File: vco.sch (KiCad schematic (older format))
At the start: 0 parts

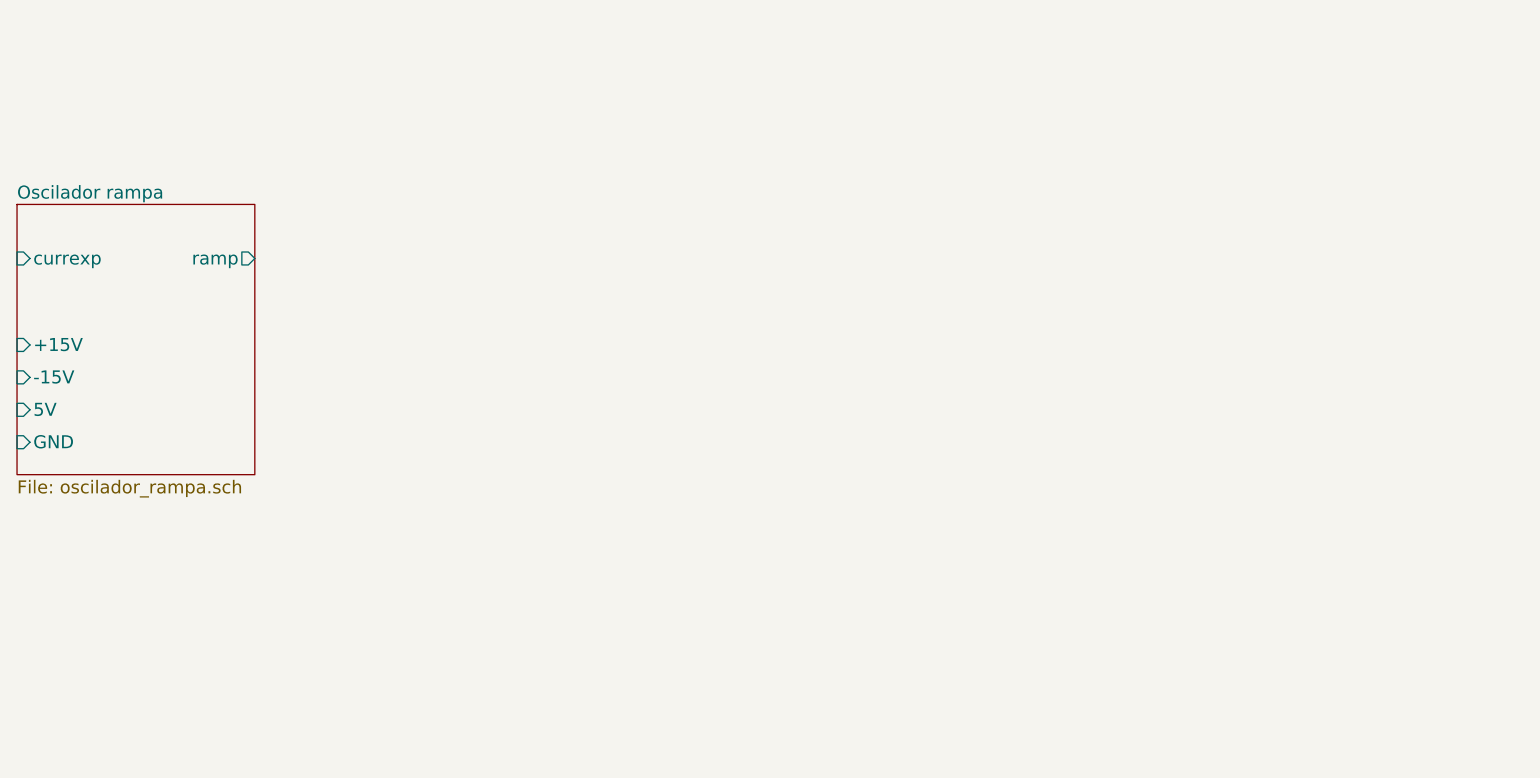
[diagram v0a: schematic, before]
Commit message: añado el conversor exponencial y mezclador
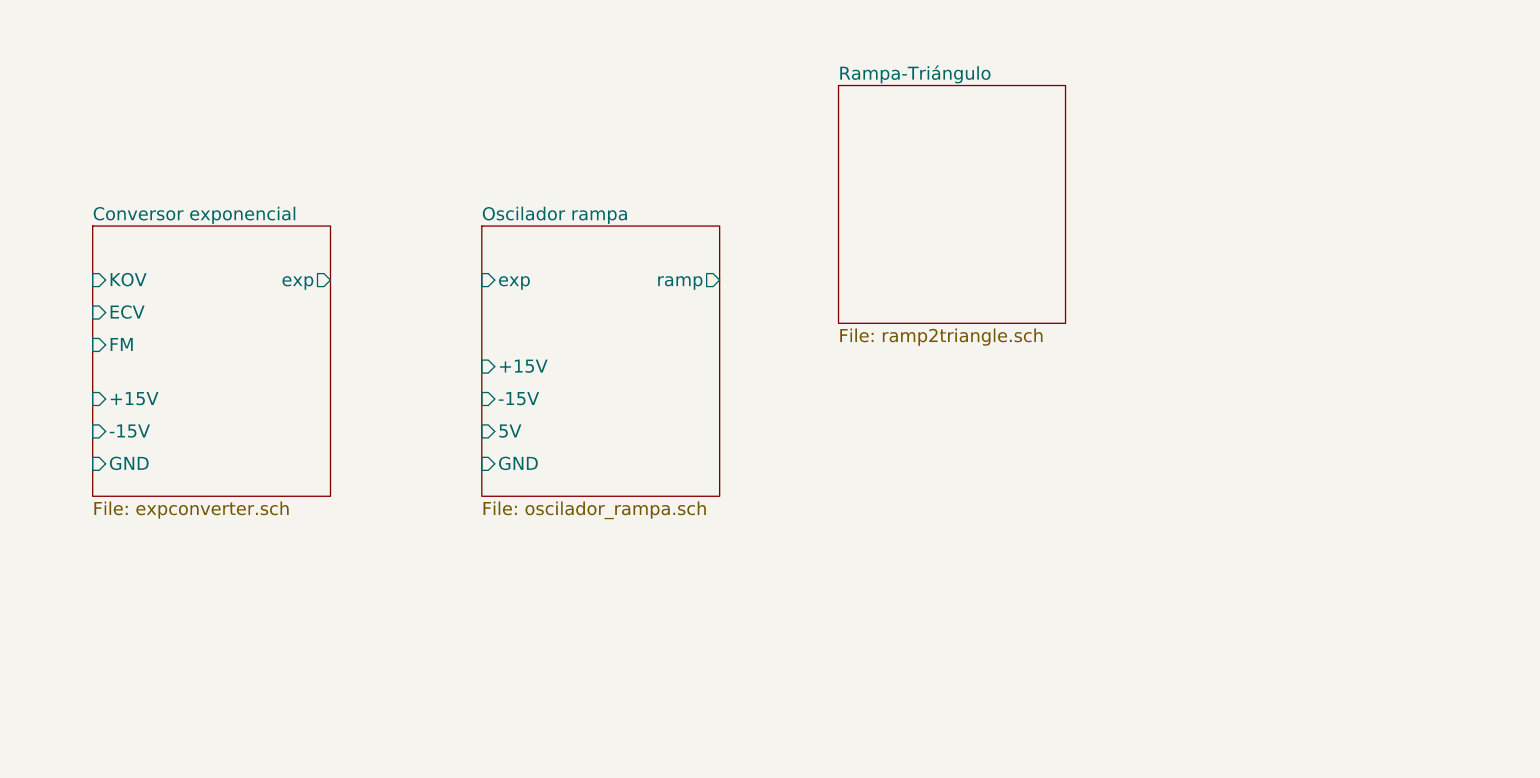
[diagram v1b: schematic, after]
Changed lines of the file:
@@
 $Descr A4 11693 8268
 encoding utf-8
-Sheet 1 2
+Sheet 1 4
 Title "Voltage Controlled Oscillator"
 Date ""
@@
 $EndDescr
 $Sheet
-S 3500 2500 1100 1250
+S 5650 2600 1100 1250
 U 59D4DFBE
 F0 "Oscilador rampa" 60
 F1 "oscilador_rampa.sch" 60
-F2 "currexp" I L 3500 2750 60
-F3 "GND" I L 3500 3600 60
-F4 "5V" I L 3500 3450 60
-F5 "ramp" O R 4600 2750 60
-F6 "+15V" I L 3500 3150 60
-F7 "-15V" I L 3500 3300 60
+F2 "exp" I L 5650 2850 60
+F3 "GND" I L 5650 3700 60
+F4 "5V" I L 5650 3550 60
+F5 "ramp" O R 6750 2850 60
+F6 "+15V" I L 5650 3250 60
+F7 "-15V" I L 5650 3400 60
+$EndSheet
+$Sheet
+S 3850 2600 1100 1250
+U 59D54B94
+F0 "Conversor exponencial" 60
+F1 "expconverter.sch" 60
+F2 "GND" I L 3850 3700 60
+F3 "KOV" I L 3850 2850 60
+F4 "ECV" I L 3850 3000 60
+F5 "FM" I L 3850 3150 60
+F6 "exp" O R 4950 2850 60
+F7 "+15V" I L 3850 3400 60
+F8 "-15V" I L 3850 3550 60
+$EndSheet
+$Sheet
+S 7300 1950 1050 1100
+U 59D5DE5D
+F0 "Rampa-Triángulo" 60
+F1 "ramp2triangle.sch" 60
 $EndSheet
 $EndSCHEMATC

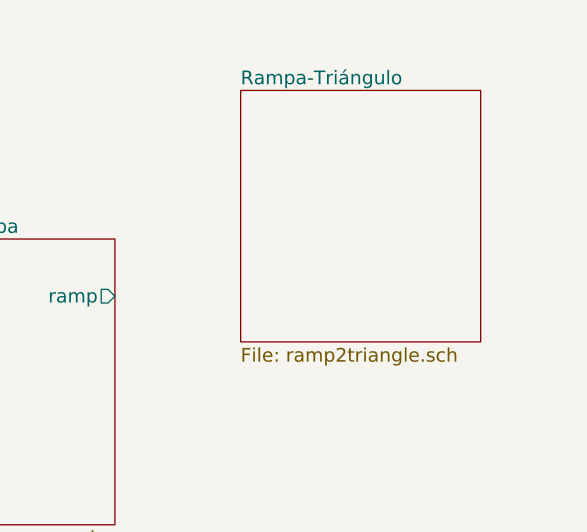
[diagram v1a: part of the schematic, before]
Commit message: sawtooh 2 triangle
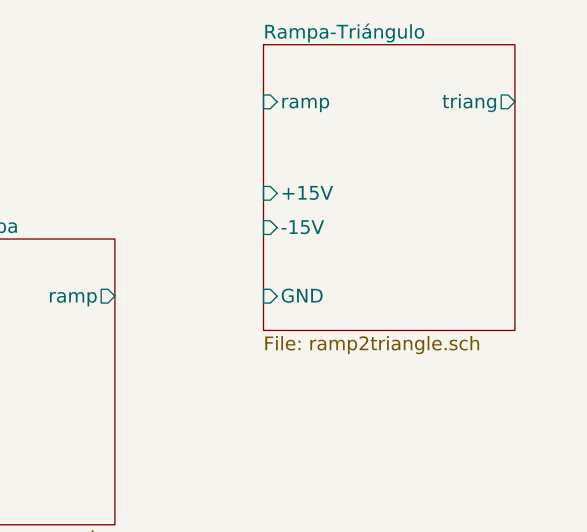
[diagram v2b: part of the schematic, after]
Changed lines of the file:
@@
 $EndSheet
 $Sheet
-S 7300 1950 1050 1100
+S 7400 1750 1100 1250
 U 59D5DE5D
 F0 "Rampa-Triángulo" 60
 F1 "ramp2triangle.sch" 60
+F2 "+15V" I L 7400 2400 60
+F3 "-15V" I L 7400 2550 60
+F4 "GND" I L 7400 2850 60
+F5 "ramp" I L 7400 2000 60
+F6 "triang" O R 8500 2000 60
 $EndSheet
 $EndSCHEMATC

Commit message: falta sumador final
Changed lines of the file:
@@
 $Descr A4 11693 8268
 encoding utf-8
-Sheet 1 4
+Sheet 1 7
 Title "Voltage Controlled Oscillator"
 Date ""
@@
 S 5650 2600 1100 1250
 U 59D4DFBE
-F0 "Oscilador rampa" 60
-F1 "oscilador_rampa.sch" 60
+F0 "sawtooh oscillator" 60
+F1 "sawtooh_osc.sch" 60
 F2 "exp" I L 5650 2850 60
 F3 "GND" I L 5650 3700 60
 F4 "5V" I L 5650 3550 60
-F5 "ramp" O R 6750 2850 60
+F5 "sawtooh" O R 6750 2850 60
 F6 "+15V" I L 5650 3250 60
 F7 "-15V" I L 5650 3400 60
@@
 S 3850 2600 1100 1250
 U 59D54B94
-F0 "Conversor exponencial" 60
+F0 "exponential converter" 60
 F1 "expconverter.sch" 60
 F2 "GND" I L 3850 3700 60
@@
 $EndSheet
 $Sheet
-S 7400 1750 1100 1250
+S 7250 2250 1100 1250
 U 59D5DE5D
-F0 "Rampa-Triángulo" 60
-F1 "ramp2triangle.sch" 60
-F2 "+15V" I L 7400 2400 60
-F3 "-15V" I L 7400 2550 60
-F4 "GND" I L 7400 2850 60
-F5 "ramp" I L 7400 2000 60
-F6 "triang" O R 8500 2000 60
+F0 "sawtooh-triangle" 60
+F1 "sawtooh2triangle.sch" 60
+F2 "+15V" I L 7250 2900 60
+F3 "-15V" I L 7250 3050 60
+F4 "GND" I L 7250 3350 60
+F5 "sawtooh" I L 7250 2500 60
+F6 "triang" O R 8350 2500 60
+$EndSheet
+$Sheet
+S 8600 2250 1100 1250
+U 59D6007F
+F0 "sawtooh-sawtooh spaced" 60
+F1 "sawtooh2sawtoothspaced.sch" 60
+F2 "+15V" I L 8600 2900 60
+F3 "-15V" I L 8600 3050 60
+F4 "GND" I L 8600 3350 60
+F5 "sawspaced" O R 9700 2500 60
+F6 "sawtooh" I L 8600 2500 60
+$EndSheet
+$Sheet
+S 8600 3700 1100 1250
+U 59D627FD
+F0 "sawtooh-sine" 60
+F1 "sawtook2sine.sch" 60
+F2 "+15V" I L 8600 4350 60
+F3 "-15V" I L 8600 4500 60
+F4 "GND" I L 8600 4800 60
+F5 "sawtooh" I L 8600 3950 60
+F6 "sine" O R 9700 3950 60
+$EndSheet
+$Sheet
+S 7250 3700 1100 1250
+U 59D64E85
+F0 "sawtooh-pwm" 60
+F1 "sawtooh2pwm.sch" 60
+F2 "+15V" I L 7250 4300 60
+F3 "-15" I L 7250 4450 60
+F4 "GND" I L 7250 4750 60
+F5 "sawtooh" I L 7250 3900 60
+F6 "PWM" I L 7250 4050 60
+F7 "pulse" O R 8350 3900 60
 $EndSheet
 $EndSCHEMATC
